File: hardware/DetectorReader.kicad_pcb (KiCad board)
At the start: 2 copper layers, 60 x 26 mm, 66 parts, among them J1 Combo_Conn, J2 CON-SMA-EDGE-S, J3 USB_C_Receptacle_USB2.0_16P, J4 CON-SMA-EDGE-S, Q1 BC847C,215, U1 XC0900P-10S, U2 ATtiny814-SS, U3 TLV70330DBVR, U4 FT231XQ, U5 MAX41460, U6 TL974IDR, U7 MAX4003, Y1 ECS-160-12-37B-CTN-TR

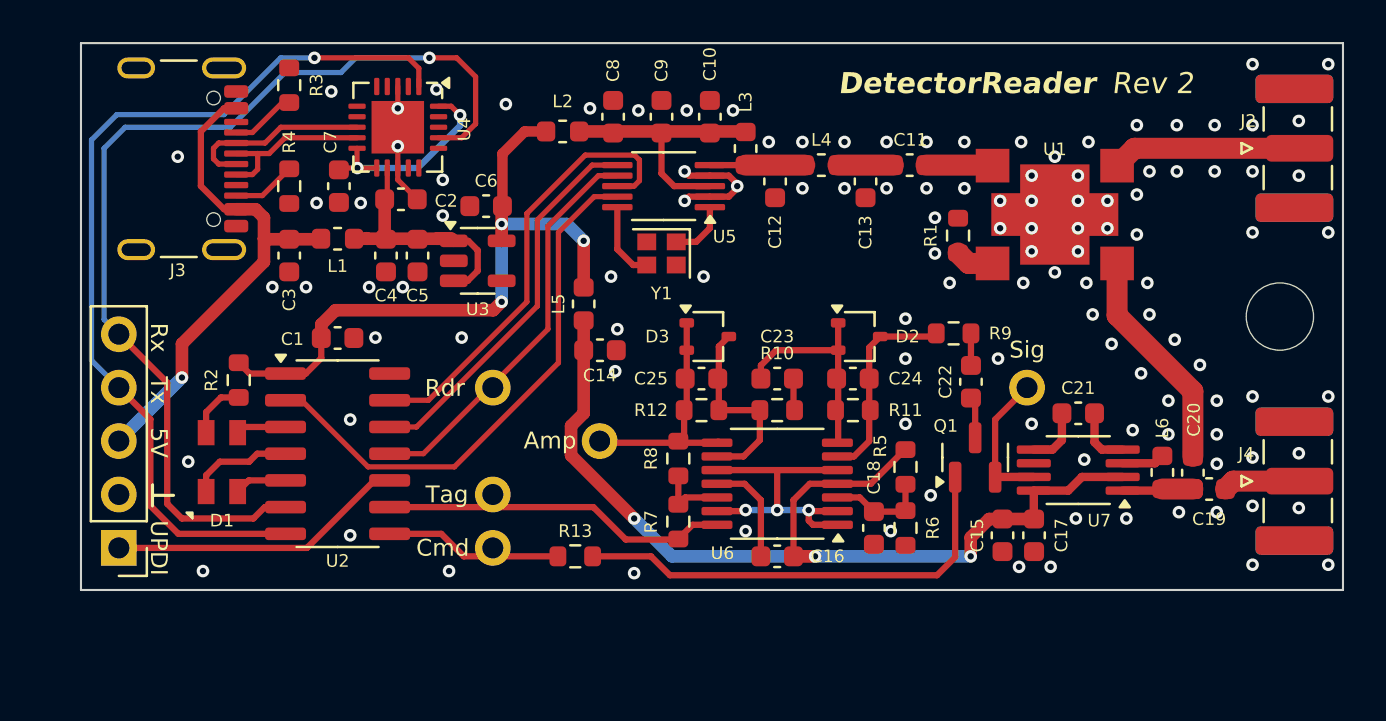
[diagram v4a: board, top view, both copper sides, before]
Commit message: Rev 3. Back to transistor-based design since op-amp approach did not work well. Using UART bridge from other brand as FTDI was sold out.
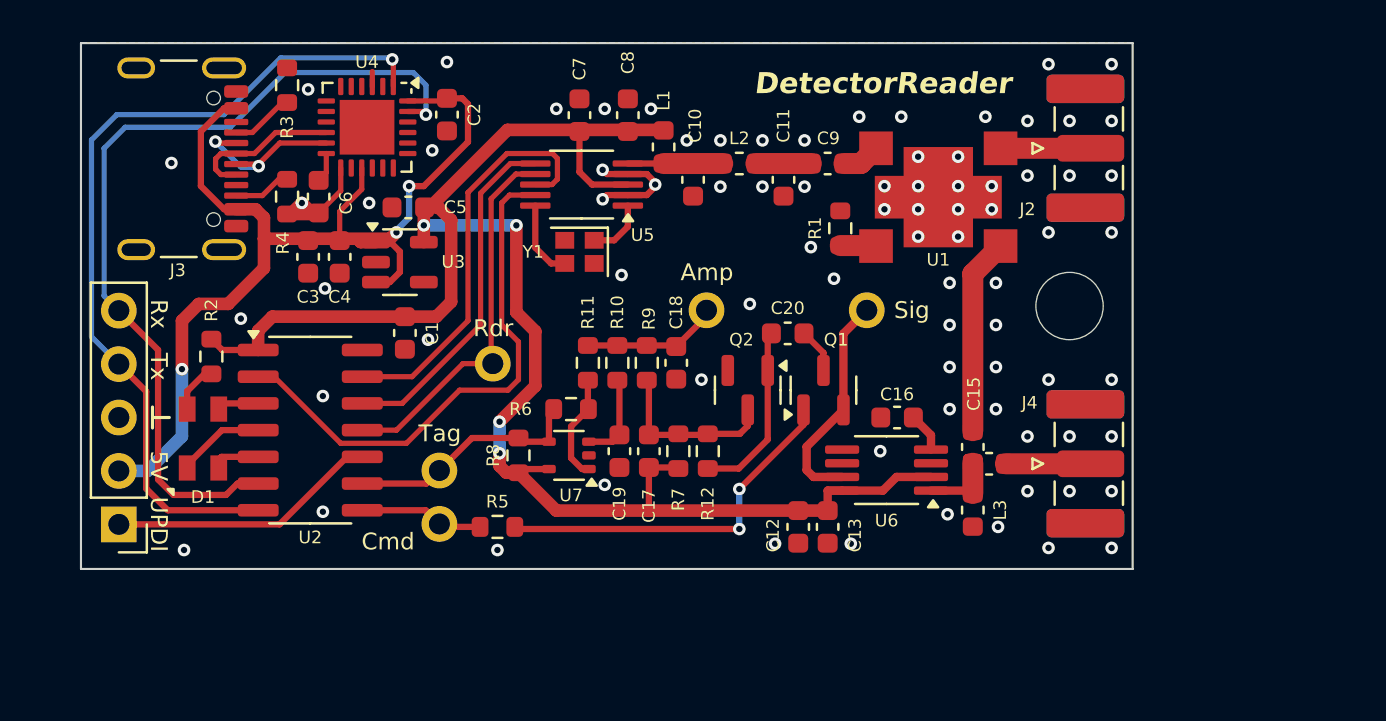
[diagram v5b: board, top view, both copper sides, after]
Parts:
- removed the C14 at (134.7, 86.6)
- removed the C15 at (153.8, 95.4)
- removed the C16 at (143.1, 96.4)
- removed C22, C23: 10n, Capacitor_SMD:C_0603_1608Metric
- removed C24, C25: 100p, Capacitor_SMD:C_0603_1608Metric
- removed the C3 at (119.9, 82.1)
- removed the C7 at (122.3, 78.8)
- removed the C8 at (135.3, 75.5)
- removed D2, D3: BAV99, Package_TO_SOT_SMD:SOT-323_SC-70
- removed the L1 at (122.2, 81.3)
- removed the L2 at (132.9, 76.2)
- removed L5: MMZ1608Y301, Inductor_SMD:L_0603_1608Metric
- removed L6: 29n, Inductor_SMD:L_0603_1608Metric
- removed the R5 at (149.2, 92.2)
- added C12: 1u, Capacitor_SMD:C_0603_1608Metric, F.Cu at (144.1, 95.0)
- added C13: 10n, Capacitor_SMD:C_0603_1608Metric, F.Cu at (145.5, 95.0)
- added C19: 100p, Capacitor_SMD:C_0603_1608Metric, F.Cu at (135.6, 91.4)
- added C20: 1u, Capacitor_SMD:C_0603_1608Metric, F.Cu at (143.6, 85.8)
- added C6: 1u, Capacitor_SMD:C_0603_1608Metric, F.Cu at (121.3, 79.3)
- added L3: 29n, Inductor_SMD:L_0603_1608Metric, F.Cu at (152.4, 94.2)
- added Q2: BC847C,215, Package_TO_SOT_SMD:SOT-23, F.Cu at (141.7, 88.5)
- C17, C18: value 10n -> 1n
- C5: renamed from C6; value 1u -> 10u
- R1: value 51 -> 50
- R10: value 1k -> 220k
- R11, R8: value 18k -> 10k
- R12: value 18k -> 220k
- R6: value 10k -> 470k
- R7: value 330k -> 1k
- U4: value FT231XQ -> CY7C65211-24LTXI; footprint Package_DFN_QFN:QFN-20-1EP_4x4mm_P0.5mm_EP2.5x2.5mm -> Package_DFN_QFN:QFN-24-1EP_4x4mm_P0.5mm_EP2.6x2.6mm
- U6: value TL974IDR -> MAX4003; footprint Package_SO:TSSOP-14_4.4x5mm_P0.65mm -> Package_SO:MSOP-8_3x3mm_P0.65mm
- U7: value MAX4003 -> LMV331; footprint Package_SO:MSOP-8_3x3mm_P0.65mm -> Package_TO_SOT_SMD:SOT-353_SC-70-5
- moved U7 24.2 mm to (133.2, 91.6)
- moved C17 18.7 mm to (137.0, 91.4)
- moved R6 16.9 mm to (133.3, 89.4), turned to 180 degrees
- moved R9 14.7 mm to (136.9, 87.2), turned to 90 degrees
- moved R11 12.8 mm to (134.1, 87.2), turned to -90 degrees
- moved C18 12.2 mm to (138.3, 87.2), turned to -90 degrees
- moved C15 10.5 mm to (152.4, 91.2)
- moved C14 10.5 mm to (153.2, 92.0)
- moved H1 10.0 mm to (157.0, 84.5)
- moved J4 9.97 mm to (158.0, 92.0)
- moved J2 9.94 mm to (158.0, 77.0)
- moved C16 8.61 mm to (148.8, 89.8)
- moved TP4 8.46 mm to (147.4, 84.7)
- moved TP5 8.03 mm to (139.7, 84.7)
- moved R10 7.93 mm to (135.5, 87.2), turned to -90 degrees
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- renumbered C12 to C10, C13 to C11, C19 to C14, C20 to C15, C21 to C16, C4 to C3, C5 to C4, C9 to C7, C10 to C8, C11 to C9, L3 to L1, L4 to L2, R13 to R5
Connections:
- C14 pad 2: Net-(U7-RF_IN) -> Net-(U6-RF_IN)
- C15 pad 1: Net-(U7-RF_IN) -> Net-(U6-RF_IN)
- C16 pad 1: Net-(U7-CLPF) -> Net-(U6-CLPF)
- C17 pad 1: GND -> +3V0
- C17 pad 2: /RF_Rx/3VRx -> /RF_Rx/AmpC
- C18 pad 1: GND -> /RF_Rx/Amp
- C18 pad 2: Net-(U6A-+) -> GND
- C7 pad 1: /RF_Tx/3VTx -> +3V0
- C8 pad 2: /RF_Tx/3VTx -> +3V0
- J1 pad 2: GND -> +5V
- J1 pad 3: /VBUS -> GND
- J3 pad A4: /VBUS -> +5V
- J3 pad A9: /VBUS -> +5V
- J3 pad B4: /VBUS -> +5V
- J3 pad B9: /VBUS -> +5V
- L1 pad 1: /RF_Tx/3VTx -> +3V0
- R10 pad 1: Net-(C23-Pad1) -> /RF_Rx/Amp
- R10 pad 2: Net-(U6C--) -> /RF_Rx/Avr
- R11 pad 1: Net-(U6B--) -> /RF_Rx/Amp
- R11 pad 2: /RF_Rx/Amp1 -> Net-(U7-+)
- R12 pad 1: Net-(U6C--) -> /RF_Rx/AmpC
- R12 pad 2: /RF_Rx/Amp2 -> Net-(Q2-B)
- R6 pad 1: Net-(U6A-+) -> Net-(U7-+)
- R6 pad 2: GND -> /TagPulses
- R7 pad 1: Net-(U6D-+) -> +3V0
- R7 pad 2: /TagPulses -> /RF_Rx/AmpC
- R8 pad 1: /RF_Rx/Amp2 -> +3V0
- R8 pad 2: Net-(U6D-+) -> /TagPulses
- R9 pad 1: Net-(C22-Pad1) -> /RF_Rx/AmpC
- R9 pad 2: Net-(U6B--) -> /RF_Rx/Amp
- TP5 pad 1: /RF_Rx/Amp2 -> /RF_Rx/Amp
- U4 pad 10: Net-(U4-3V3OUT) -> /USB_P
- U4 pad 11: Net-(U4-3V3OUT) -> /USB_N
- U4 pad 12: +5V -> Net-(U4-VCCD)
- U4 pad 15: unconnected-(U4-CBUS0-Pad15) -> +5V
- U4 pad 16: unconnected-(U4-CBUS3-Pad16) -> GND
- U4 pad 17: /uartRx -> GND
- U4 pad 20: Net-(U4-3V3OUT) -> unconnected-(U4-SCB_1/GPIO_2-Pad20)
- U4 pad 21: GND -> unconnected-(U4-SCB_2/GPIO_3-Pad21)
- U4 pad 8: /USB_N -> unconnected-(U4-SUSPEND-Pad8)
- U4 pad 9: /USB_P -> unconnected-(U4-WAKEUP-Pad9)
- U5 pad 3: /RF_Tx/3VTx -> +3V0
- U6 pad 1: /RF_Rx/CM -> Net-(U6-RF_IN)
- U6 pad 2: /RF_Rx/CM -> +3V0
- U6 pad 3: Net-(U6A-+) -> GND
- U6 pad 4: /RF_Rx/3VRx -> Net-(U6-CLPF)
- U6 pad 5: /RF_Rx/CM -> GND
- U6 pad 6: Net-(U6B--) -> unconnected-(U6-NC-Pad6)
- U6 pad 7: /RF_Rx/Amp1 -> /RF_Rx/Signal
- U6 pad 8: /RF_Rx/Amp2 -> +3V0
- U7 pad 1: Net-(U7-RF_IN) -> Net-(U7-+)
- U7 pad 2: /RF_Rx/3VRx -> GND
- U7 pad 3: GND -> /RF_Rx/Avr
- U7 pad 4: Net-(U7-CLPF) -> /TagPulses
- U7 pad 5: GND -> +3V0
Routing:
- net +3V0: track 31.9 -> 81.8 mm, vias 3 -> 4
- net /RF_Rx/3VRx: track 47.8 -> 0.00 mm, vias 3 -> 0
- net +5V: track 12.4 -> 51.3 mm, vias 0 -> 3
- net /VBUS: track 24.6 -> 0.00 mm, vias 1 -> 0
- net /RF_Rx/CM: track 15.4 -> 0.00 mm, vias 3 -> 0
- net /RF_Tx/3VTx: track 12.4 -> 0.00 mm
- net /RF_Rx/Amp2: track 10.9 -> 0.00 mm
- net /RF_Rx/Amp1: track 10.3 -> 0.00 mm
- net Net-(U4-3V3OUT): track 10.2 -> 0.00 mm, vias 2 -> 0
- net Net-(U6B--): track 9.73 -> 0.00 mm
- net Net-(U6C--): track 9.43 -> 0.00 mm
- net GND: track 21.4 -> 12.4 mm, vias 117 -> 80
- net Net-(Q2-B): track 0.00 -> 8.54 mm
- net /RF_Rx/AmpC: track 0.00 -> 8.28 mm
- net /uartRx: track 48.4 -> 41.5 mm
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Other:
- board size 60 x 26 mm -> 50 x 25 mm
- board text removed: "Rev 2"

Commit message: Rev 4. Removed coupler and detector IC. Using simple diode as detector.
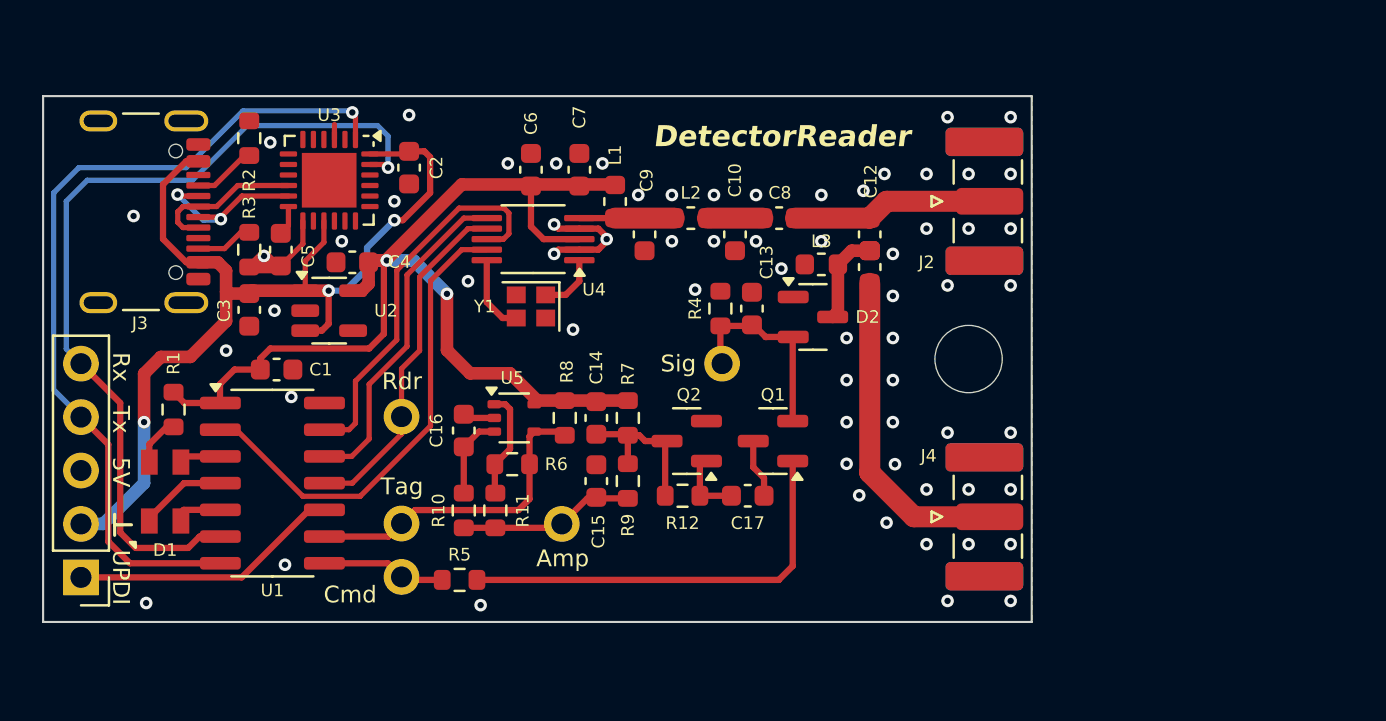
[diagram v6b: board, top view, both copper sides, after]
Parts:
- removed the C12 at (144.1, 95.0)
- removed the C13 at (145.5, 95.0)
- removed the C4 at (122.3, 82.2)
- removed the R1 at (146.1, 80.8)
- removed the U1 at (150.8, 79.3)
- removed U6: MAX4003, Package_SO:MSOP-8_3x3mm_P0.65mm
- added D2: BAT54S, Package_TO_SOT_SMD:SOT-23, F.Cu at (144.8, 85.0)
- added R4: 5.1k, Resistor_SMD:R_0603_1608Metric, F.Cu at (140.4, 84.6)
- C11: renamed from C14; value 1.2p -> 10p
- C12: renamed from C15; value 1.2p -> 10p
- C17: renamed from C20; value 1u -> 10n
- L3: value 29n -> 22n
- R6: value 470k -> 1M
- R8: value 10k -> 1k
- moved L3 13.7 mm to (145.2, 82.5), turned to 180 degrees
- moved TP5 12.3 mm to (132.9, 94.9)
- moved C12 11.2 mm to (147.5, 81.1)
- moved C11 10.9 mm to (147.5, 82.6), turned to 90 degrees
- moved R10 10.1 mm to (128.2, 94.2), turned to 90 degrees
- moved C13 8.63 mm to (141.9, 84.6), turned to 90 degrees
- moved R11 8.28 mm to (129.7, 94.2), turned to 90 degrees
- moved C17 7.95 mm to (141.7, 93.5)
- moved C16 7.46 mm to (128.2, 90.4), turned to 90 degrees
- moved TP4 7.33 mm to (140.5, 87.2)
- moved C15 6.78 mm to (134.5, 92.8), turned to 90 degrees
- moved C1 6.34 mm to (119.3, 87.5), turned to 180 degrees
- moved R9 5.69 mm to (136.0, 92.8), turned to -90 degrees
- moved H1 5.42 mm to (152.2, 87.0)
- moved J2 5.42 mm to (153.2, 79.5)
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- renumbered C11 to C10, C16 to C13, C17 to C14, C18 to C15, C19 to C16, C5 to C4, C6 to C5, C7 to C6, C8 to C7, C9 to C8, C10 to C9, R2 to R1, R3 to R2, R4 to R3, U2 to U1, U3 to U2, U4 to U3, U5 to U4, U7 to U5
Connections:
- C13 pad 1: Net-(U6-CLPF) -> /RF_Rx/Signal
- C8 pad 1: /RF_Tx/RfOut -> /RF_Rx/DetectorIn
- J2 pad 1: Net-(J2-In) -> /RF_Rx/DetectorIn
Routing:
- net +3V0: track 81.8 -> 52.4 mm, vias 4 -> 2
- net Net-(J4-In): track 4.05 -> 15.6 mm
- net Net-(Q2-B): track 8.54 -> 3.15 mm
- net Net-(J2-In): track 4.28 -> 0.00 mm
- net /TagPulses: track 11.5 -> 15.3 mm
- net +5V: track 51.3 -> 48.2 mm
- net Net-(Q1-B): track 17.6 -> 20.3 mm, vias 2 -> 0
- net /SPI.~{CS}: track 25.4 -> 22.9 mm
- net Net-(U6-CLPF): track 1.87 -> 0.00 mm
- net /SPI.MOSI: track 18.0 -> 16.1 mm
- net /RF_Rx/Amp: track 6.54 -> 8.38 mm
- net /RF_Tx/RfOut: track 1.83 -> 0.00 mm
- net Net-(U1-CPL): track 1.71 -> 0.00 mm
- net GND: track 12.4 -> 14.0 mm, vias 80 -> 65
- net /RF_Rx/Signal: track 10.6 -> 9.53 mm
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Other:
- board size 50 x 25 mm -> 47 x 25 mm

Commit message: Fixed UART bridge power supply. Made board 1 mm shorter.
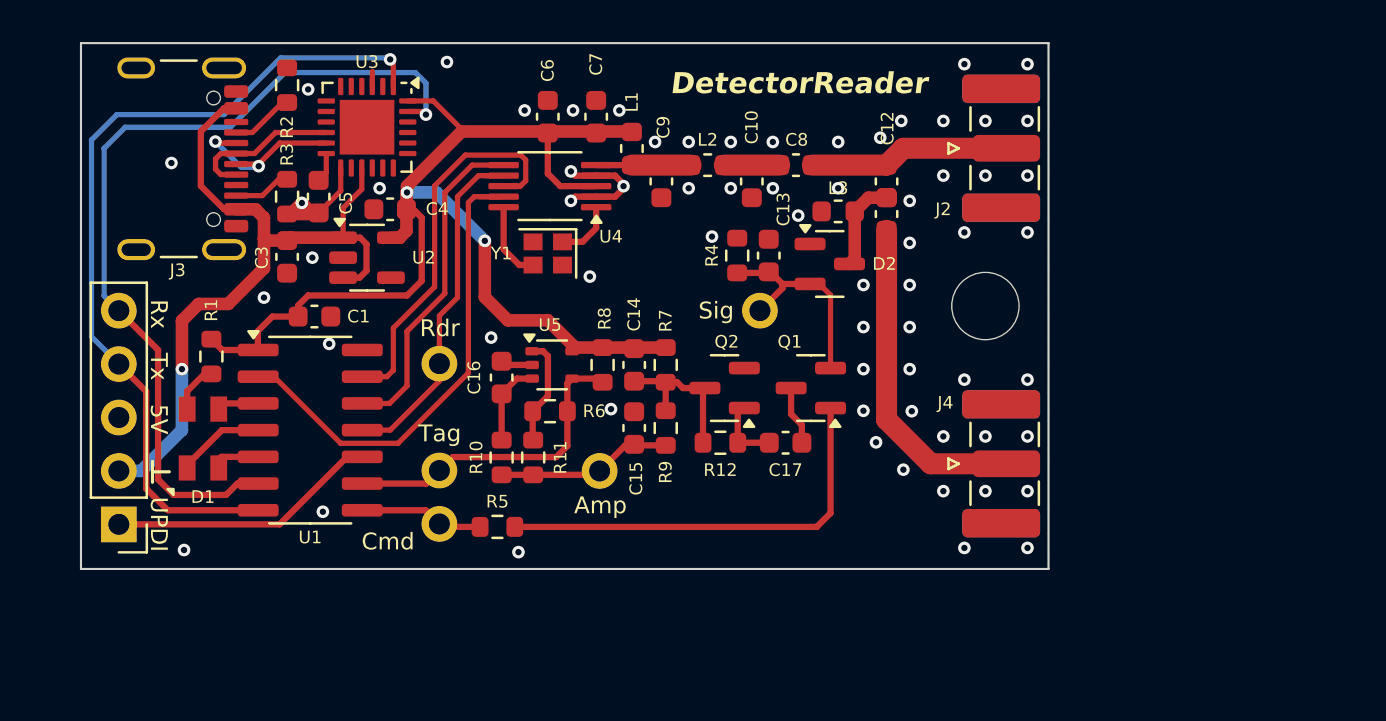
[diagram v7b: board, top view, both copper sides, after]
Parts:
- removed C2: 100n, Capacitor_SMD:C_0603_1608Metric
- moved TP1 3.10 mm to (127.0, 87.2)
- moved TP3 3.10 mm to (127.0, 92.3)
- moved C3 3.10 mm to (119.8, 82.2)
- moved J1 3.10 mm to (111.8, 94.9)
- moved C14 3.10 mm to (136.3, 87.3)
- moved C15 3.10 mm to (136.3, 90.3)
- moved C16 3.10 mm to (130.0, 87.9)
- moved C17 3.10 mm to (143.5, 91.0)
- moved R10 3.10 mm to (130.0, 91.7)
- moved R11 3.10 mm to (131.5, 91.7)
- moved R12 3.10 mm to (140.4, 91.0)
- moved R5 3.10 mm to (129.8, 95.0)
- moved R6 3.10 mm to (132.3, 89.5)
- moved R7 3.10 mm to (137.8, 87.3)
- moved R8 3.10 mm to (134.8, 87.3)
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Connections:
- U3 pad 24: +5V -> +3V0
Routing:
- net +5V: track 48.2 -> 36.0 mm, vias 3 -> 1
- net +3V0: track 52.4 -> 55.7 mm
- net /SPI.MOSI: track 16.1 -> 16.9 mm
- net /SPI.~{CS}: track 22.9 -> 23.6 mm
- net /RF_Rx/Signal: track 9.53 -> 10.2 mm
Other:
- board size 47 x 25 mm -> 46 x 25 mm

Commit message: Fixed connector pinout according to silkscreen
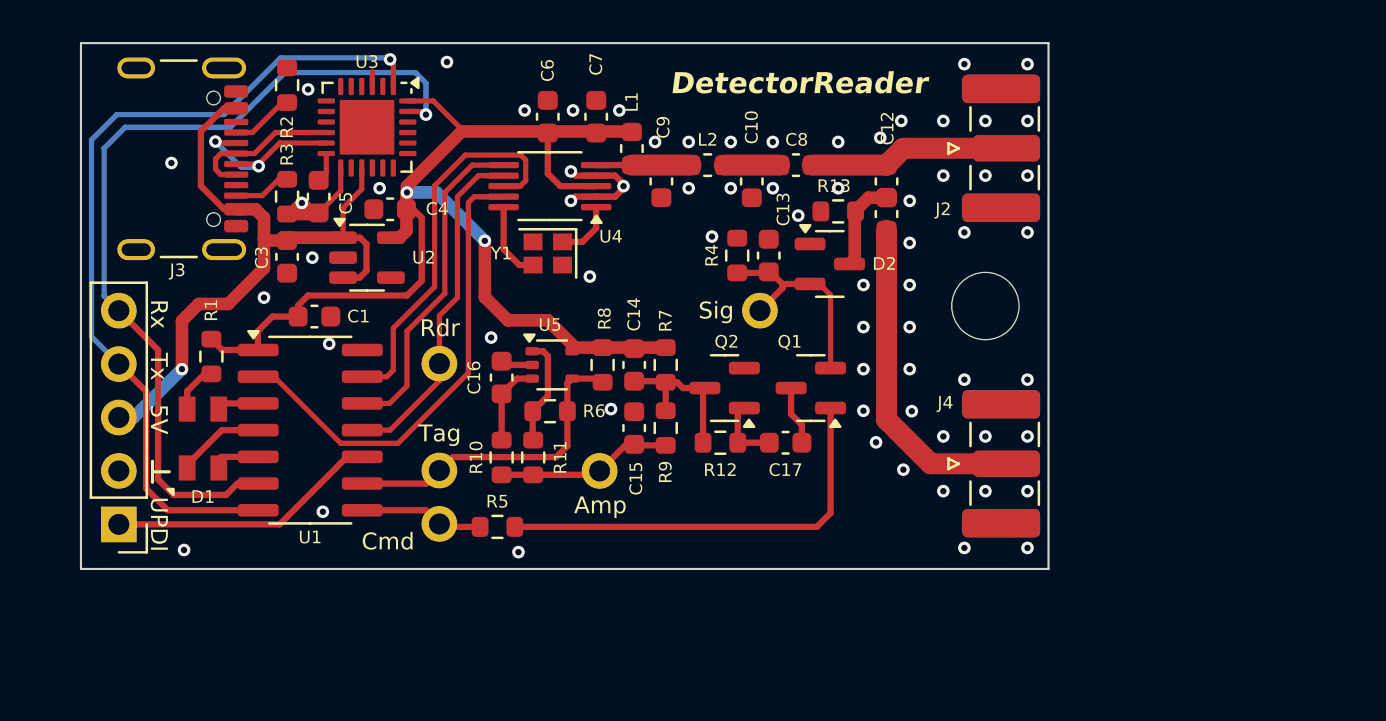
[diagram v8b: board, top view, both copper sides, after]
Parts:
- C12: value 10p -> 2.7p
- R13: renamed from L3; value 22n -> 50R; footprint Inductor_SMD:L_0603_1608Metric -> Resistor_SMD:R_0603_1608Metric
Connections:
- J1 pad 2: +5V -> GND
- J1 pad 3: GND -> +5V
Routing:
- net +5V: track 36.0 -> 33.3 mm
